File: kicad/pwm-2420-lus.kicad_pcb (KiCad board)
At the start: 2 copper layers, 90 x 85 mm, 127 parts, among them J1 MKDS 5/ 2-9,5, J2 MKDS 5/ 2-9,5, J3 MKDS 5/ 2-9,5, J4 UEXT, J5 USB_A, J6 PWR_12V, J7 6P6C, J8 ST_Nucleo_SWD_5p, Q1 PSMN7R5-60YLX, Q2 PSMN7R5-60YLX, Q3 PSMN7R5-60YLX, Q6 IRFB7787, Q7 IRFB7787, Q8 IRFB7787, T1 MMBT3904, T2 MMBT3906, T3 MMBT3904, T4 MMBT3904, T5 MMBT3904, U1 STM32L072CZTx, U2 TLV9002, U3 MC34063AD, U4 D1213A-04SO, U5 LP2950-3.3_TO252

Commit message: Folder restructured and files renamed
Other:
- board text removed: "~RESET"

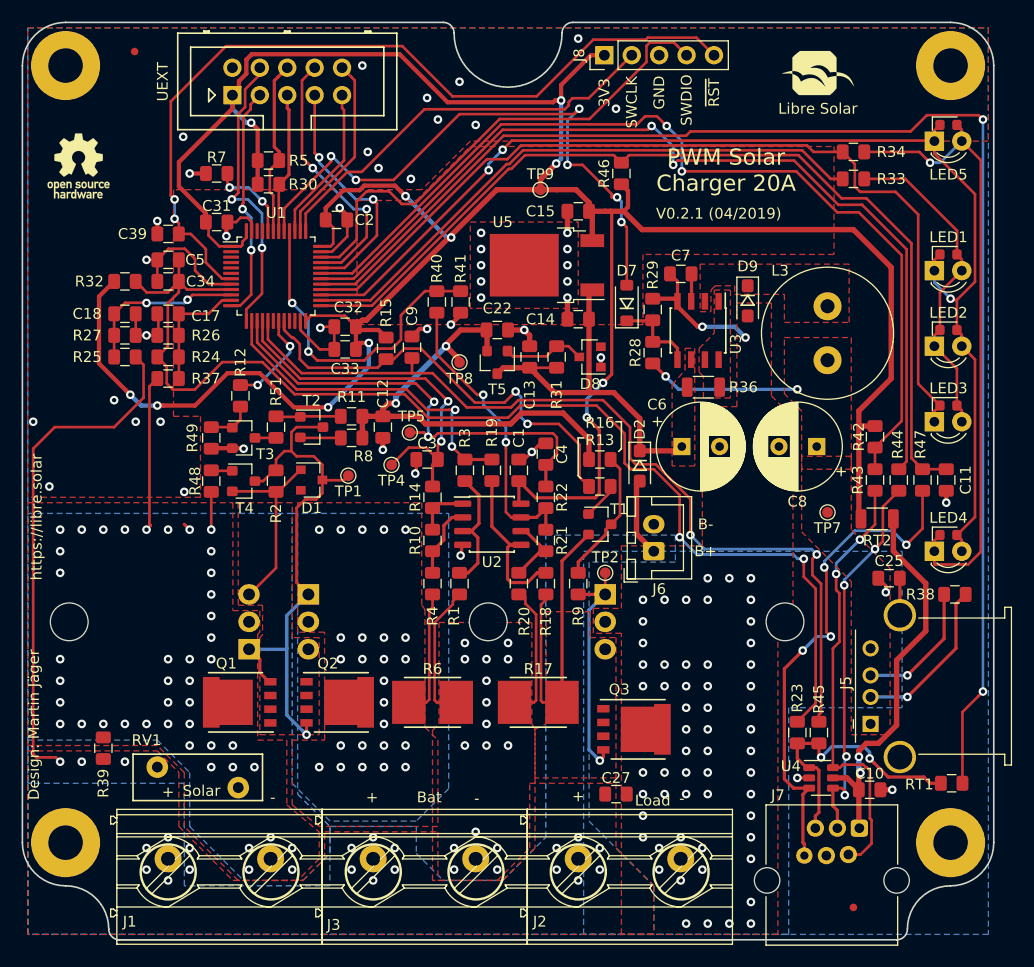
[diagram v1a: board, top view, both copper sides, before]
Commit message: Load current sense filter and comparator updated
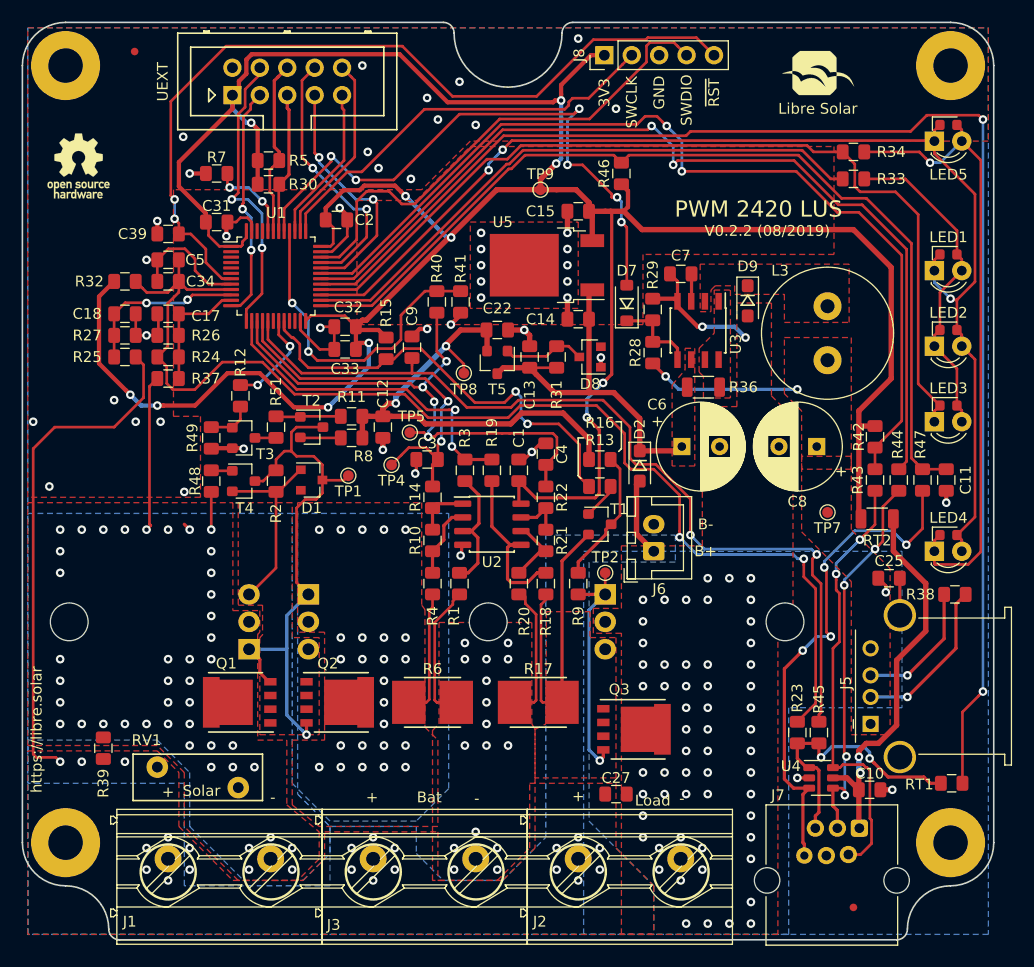
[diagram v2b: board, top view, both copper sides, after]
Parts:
- R22: value 2.2k -> 39k
- moved TP8 1.08 mm to (139.4, 85.5)
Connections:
- R40 pad 2: Net-(R21-Pad2) -> I_LOAD
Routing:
- net Net-(R21-Pad2): track 27.8 -> 4.76 mm, vias 2 -> 0
- net I_LOAD: track 43.2 -> 51.6 mm, vias 2 -> 4
- net +12V: track 44.4 -> 45.5 mm
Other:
- board text added: "PWM 2420 LUS"
- board text added: "V0.2.2 (08/2019)"
- board text removed: "Design: Martin Jäger"
- board text removed: "PWM Solar Charger 20A"
- board text removed: "V0.2.1 (04/2019)"
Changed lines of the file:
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@@
-(kicad_pcb (version 20171130) (host pcbnew 5.1.0)
+(kicad_pcb (version 20171130) (host pcbnew 5.1.2)
   (general
     (thickness 1.6)
-    (drawings 81)
-    (tracks 1282)
+    (drawings 80)
+    (tracks 1278)
     (zones 0)
     (modules 127)
@@
     )
     (pad 2 smd roundrect (at 1 0 270) (size 1.1 1.4) (layers Top F.Paste F.Mask) (roundrect_rratio 0.2)
-      (net 52 "Net-(R21-Pad2)"))
+      (net 28 I_LOAD))
     (pad 1 smd roundrect (at -1 0 270) (size 1.1 1.4) (layers Top F.Paste F.Mask) (roundrect_rratio 0.2)
       (net 60 I_LOAD_COMP))
@@
       (effects (font (size 1 1) (thickness 0.15)))
     )
-    (fp_text value 2.2k (at 0 1.75 90) (layer F.Fab)
+    (fp_text value 39k (at 0 1.75 90) (layer F.Fab)
       (effects (font (size 1 1) (thickness 0.15)))
     )
@@
   )
   (module TestPoint:TestPoint_Pad_D1.0mm (layer Top)
-    (at 139 84.5)
+    (at 139.4 85.5)
     (descr "SMD pad as test Point, diameter 1.0mm")
     (tags "test point SMD pad")
@@
     (effects (font (size 1.5 1.5) (thickness 0.3)) (justify mirror))
   )
-  (gr_text "V0.2.1 (04/2019)" (at 157.2 71.3) (layer F.SilkS)
+  (gr_text "V0.2.2 (08/2019)" (at 161.7 72.9) (layer F.SilkS)
     (effects (font (size 1 1) (thickness 0.15)) (justify left bottom))
   )
-  (gr_text "PWM Solar\nCharger 20A" (at 163.7 66.7) (layer F.SilkS)
+  (gr_text "PWM 2420 LUS" (at 166.7 70.3) (layer F.SilkS)
     (effects (font (size 1.5 1.5) (thickness 0.3)))
   )
@@
   (gr_line (start 107.5 138) (end 179.5 138) (angle 90) (layer Edge.Cuts) (width 0.15))
   (gr_arc (start 102.5 129) (end 102.5 133) (angle 90) (layer Edge.Cuts) (width 0.15))
-  (gr_text "Design: Martin Jäger" (at 100.15 125.05 90) (layer F.SilkS)
-    (effects (font (size 1 1) (thickness 0.15)) (justify left bottom))
-  )
-  (gr_text https://libre.solar (at 100.4 104.7 90) (layer F.SilkS)
+  (gr_text https://libre.solar (at 100.4 124.4 90) (layer F.SilkS)
     (effects (font (size 1 1) (thickness 0.15)) (justify left bottom))
   )
@@
   (segment (start 147 96) (end 147 94) (width 0.3) (layer Top) (net 28))
   (via (at 136.649995 88.149995) (size 0.8) (drill 0.4) (layers Top Bottom) (net 28))
-  (segment (start 134.949991 86.449991) (end 136.299996 87.799996) (width 0.25) (layer Top) (net 28))
-  (segment (start 120.25 82.658002) (end 124.041989 86.449991) (width 0.25) (layer Top) (net 28))
-  (segment (start 124.041989 86.449991) (end 134.949991 86.449991) (width 0.25) (layer Top) (net 28))
-  (segment (start 136.299996 87.799996) (end 136.649995 88.149995) (width 0.25) (layer Top) (net 28))
-  (segment (start 120.25 80.6625) (end 120.25 82.658002) (width 0.25) (layer Top) (net 28))
-  (segment (start 136.1 90.90503) (end 136.1 91.400004) (width 0.25) (layer Bottom) (net 28))
-  (segment (start 136.1 88.69999) (end 136.1 90.90503) (width 0.25) (layer Bottom) (net 28))
   (segment (start 135.750001 91.050005) (end 136.1 91.400004) (width 0.25) (layer Top) (net 28))
   (segment (start 135.699996 91) (end 135.750001 91.050005) (width 0.25) (layer Top) (net 28))
   (segment (start 134.4 91) (end 135.699996 91) (width 0.25) (layer Top) (net 28))
   (via (at 136.1 91.400004) (size 0.8) (drill 0.4) (layers Top Bottom) (net 28))
-  (segment (start 136.649995 88.149995) (end 136.1 88.69999) (width 0.25) (layer Bottom) (net 28))
   (segment (start 136.990666 91.075023) (end 136.665685 91.400004) (width 0.25) (layer Top) (net 28))
   (segment (start 136.665685 91.400004) (end 136.1 91.400004) (width 0.25) (layer Top) (net 28))
@@
   (segment (start 147 94) (end 148.02501 92.97499) (width 0.25) (layer Top) (net 28))
   (segment (start 143.648002 91.074998) (end 142.951998 91.074998) (width 0.25) (layer Top) (net 28))
+  (via (at 137.8 84.4) (size 0.8) (drill 0.4) (layers Top Bottom) (net 28))
+  (segment (start 137.8 84.4) (end 135.6 86.6) (width 0.25) (layer Bottom) (net 28))
+  (via (at 135.6 86.8) (size 0.8) (drill 0.4) (layers Top Bottom) (net 28))
+  (segment (start 135.6 86.6) (end 135.6 86.8) (width 0.25) (layer Bottom) (net 28))
+  (segment (start 136.649995 87.849995) (end 135.6 86.8) (width 0.25) (layer Top) (net 28))
+  (segment (start 136.649995 88.149995) (end 136.649995 87.849995) (width 0.25) (layer Top) (net 28))
+  (segment (start 134.8 86.8) (end 135.6 86.8) (width 0.25) (layer Top) (net 28))
+  (segment (start 134.449991 86.449991) (end 134.8 86.8) (width 0.25) (layer Top) (net 28))
+  (segment (start 124.041989 86.449991) (end 134.449991 86.449991) (width 0.25) (layer Top) (net 28))
+  (segment (start 120.25 80.6625) (end 120.25 82.658002) (width 0.25) (layer Top) (net 28))
+  (segment (start 120.25 82.658002) (end 124.041989 86.449991) (width 0.25) (layer Top) (net 28))
+  (segment (start 136.1 90.90503) (end 136.1 91.400004) (width 0.25) (layer Bottom) (net 28))
+  (segment (start 136.7 90.30503) (end 136.1 90.90503) (width 0.25) (layer Bottom) (net 28))
+  (segment (start 136.649995 88.149995) (end 136.7 88.2) (width 0.25) (layer Bottom) (net 28))
+  (segment (start 136.7 88.2) (end 136.7 90.30503) (width 0.25) (layer Bottom) (net 28))
+  (segment (start 136.9 83.5) (end 137.8 84.4) (width 0.25) (layer Top) (net 28))
+  (segment (start 136.9 79.9) (end 136.9 83.5) (width 0.25) (layer Top) (net 28))
   (segment (start 143.940501 83.940501) (end 143.45 83.45) (width 0.25) (layer Top) (net 29))
   (segment (start 147.059499 83.940501) (end 143.940501 83.940501) (width 0.25) (layer Top) (net 29))
@@
   (segment (start 146.135 98.865) (end 147 98) (width 0.3) (layer Top) (net 52))
   (segment (start 144.6 98.865) (end 146.135 98.865) (width 0.3) (layer Top) (net 52))
-  (via (at 141.2 87.499996) (size 0.8) (drill 0.4) (layers Top Bottom) (net 52))
-  (segment (start 136.9 79.9) (end 136.9 83.765681) (width 0.25) (layer Top) (net 52))
-  (segment (start 136.9 83.765681) (end 140.634315 87.499996) (width 0.25) (layer Top) (net 52))
-  (segment (start 140.634315 87.499996) (end 141.2 87.499996) (width 0.25) (layer Top) (net 52))
-  (segment (start 144.7 98.865) (end 143.8 98.865) (width 0.25) (layer Top) (net 52))
-  (segment (start 143.8 98.865) (end 143.3 98.365) (width 0.25) (layer Top) (net 52))
-  (segment (start 143.3 92.465689) (end 143.3 91.900004) (width 0.25) (layer Top) (net 52))
-  (segment (start 143.3 98.365) (end 143.3 92.465689) (width 0.25) (layer Top) (net 52))
-  (via (at 143.3 91.900004) (size 0.8) (drill 0.4) (layers Top Bottom) (net 52))
-  (segment (start 143.3 91.334319) (end 143.3 91.900004) (width 0.25) (layer Bottom) (net 52))
-  (segment (start 143.3 90.5) (end 143.3 91.334319) (width 0.25) (layer Bottom) (net 52))
-  (segment (start 141.2 87.499996) (end 141.2 88.4) (width 0.25) (layer Bottom) (net 52))
-  (segment (start 141.2 88.4) (end 143.3 90.5) (width 0.25) (layer Bottom) (net 52))
   (via (at 132 114) (size 0.8) (drill 0.4) (layers Top Bottom) (net 53))
   (via (at 132 116) (size 0.8) (drill 0.4) (layers Top Bottom) (net 53))
@@
   (segment (start 141.55 81.55) (end 141.5 81.5) (width 0.5) (layer Top) (net 79))
   (segment (start 141.55 83.45) (end 141.55 81.55) (width 0.5) (layer Top) (net 79))
-  (segment (start 139 84.25) (end 137.75 83) (width 0.5) (layer Top) (net 79))
-  (segment (start 139 84.5) (end 139 84.25) (width 0.5) (layer Top) (net 79))
   (segment (start 141.5 81.5) (end 139.1 81.5) (width 0.5) (layer Top) (net 79))
   (segment (start 137.75 82.85) (end 137.75 83) (width 0.5) (layer Top) (net 79))
@@
   (segment (start 151 91.6) (end 148.599998 89.199998) (width 0.5) (layer Top) (net 79))
   (segment (start 135.150401 89.5) (end 132.7 89.5) (width 0.5) (layer Top) (net 79))
+  (segment (start 139.4 84.65) (end 137.75 83) (width 0.25) (layer Top) (net 79))
+  (segment (start 139.4 85.5) (end 139.4 84.65) (width 0.25) (layer Top) (net 79))
   (segment (start 185.54 62.9525) (end 185.0875 62.5) (width 0.25) (layer Top) (net 80))
   (segment (start 185.54 64) (end 185.54 62.9525) (width 0.25) (layer Top) (net 80))

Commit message: Improved power supply and exposed BOOT0 pin
- BOOT0 pin connected to BUTTON wire to allow firmware upgrade via LS.one port
- Additional emitter follower for 3V3 power supply to increase margin to 30V absolute max. rating of LDO in case of 24V battery
- Corners adjusted to match shape of MPPT 1210 HUS
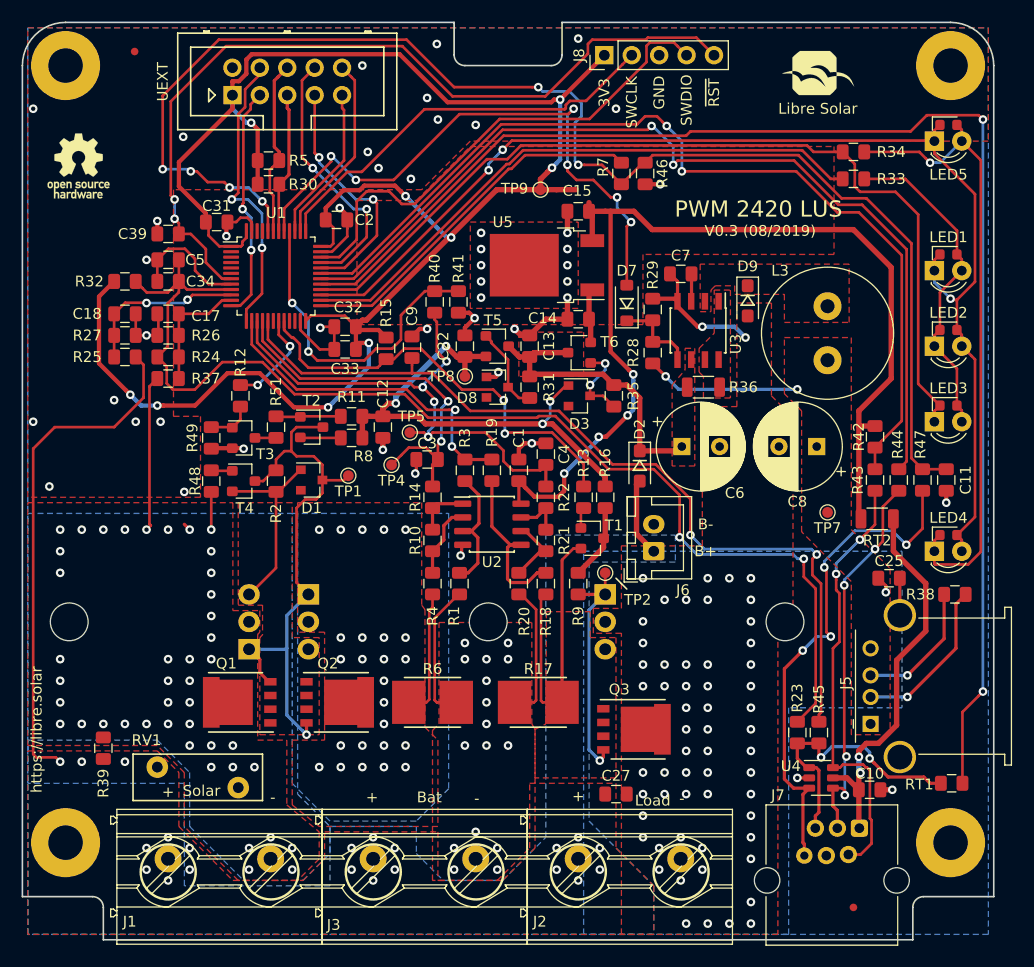
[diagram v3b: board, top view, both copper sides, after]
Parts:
- added D3: 12V, Diode_SMD:D_SOT-23_ANK, F.Cu at (150.1, 87.6)
- added R35: 12k, LibreSolar:R_0805_2012, F.Cu at (153.3, 87.6)
- added T6: MMBT3904, LibreSolar:SOT-23, F.Cu at (150.1, 83.6)
- Q6, Q7, Q8: value IRFB7787 -> AOT266L
- moved R7 37.5 mm to (154.0, 67.0), turned to 270 degrees
- moved D8 9.04 mm to (142.5, 86.8), turned to 0 degrees
- moved R31 3.75 mm to (145.5, 86.8), turned to 90 degrees
- moved R16 3.54 mm to (152.5, 97.0), turned to 90 degrees
- moved C22 3.35 mm to (139.5, 83.0), turned to 90 degrees
- moved R46 2.20 mm to (156.2, 67.0), turned to 270 degrees
- moved R13 1.80 mm to (150.5, 97.0), turned to 90 degrees
- moved T5 1.50 mm to (142.5, 83.0), turned to 0 degrees
- moved T1 1.48 mm to (151.3, 100.8)
- moved C13 1.00 mm to (145.5, 83.0)
- moved TP8 0.32 mm to (139.5, 85.8)
- moved R40 0.20 mm to (136.7, 78.9)
- moved R41 0.20 mm to (138.9, 78.9)
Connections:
- C11 pad 1: /MCU/BUTTON -> /MCU/BOOT0
- C13 pad 1: Net-(C13-Pad1) -> /Power Supply/BAT_INPUT
- C14 pad 1: Net-(C13-Pad1) -> Net-(C14-Pad1)
- C6 pad 1: Net-(C13-Pad1) -> /Power Supply/BAT_INPUT
- D2 pad 1: Net-(C13-Pad1) -> /Power Supply/BAT_INPUT
- MK2 pad 1: GND -> Net-(MK2-Pad1)
- MK3 pad 1: GND -> Net-(MK3-Pad1)
- MK4 pad 1: GND -> Net-(MK4-Pad1)
- R31 pad 2: Net-(C13-Pad1) -> /Power Supply/BAT_INPUT
- R36 pad 2: Net-(C13-Pad1) -> /Power Supply/BAT_INPUT
- R46 pad 1: +3V3 -> /MCU/BOOT0
- R46 pad 2: /MCU/BUTTON -> GND
- R47 pad 2: /MCU/BUTTON -> /MCU/BOOT0
- R7 pad 1: /MCU/BOOT0 -> /MCU/BUTTON
- R7 pad 2: GND -> /MCU/BOOT0
- T5 pad 3: Net-(C13-Pad1) -> /Power Supply/BAT_INPUT
- U3 pad 6: Net-(C13-Pad1) -> /Power Supply/BAT_INPUT
- U5 pad 1: Net-(C13-Pad1) -> Net-(C14-Pad1)
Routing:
- net /MCU/BOOT0: track 7.92 -> 129.4 mm, vias 2 -> 6
- net /MCU/BUTTON: track 88.0 -> 33.9 mm
- net Net-(C13-Pad1): track 34.6 -> 0.00 mm
- net /Power Supply/BAT_INPUT: track 0.00 -> 28.0 mm
- net Net-(D3-Pad1): track 0.00 -> 7.56 mm, vias 0 -> 2
- net GND: track 89.6 -> 96.0 mm, vias 62 -> 63
- net +3V3: track 283.1 -> 277.1 mm, vias 11 -> 13
- net Net-(R16-Pad1): track 12.5 -> 7.04 mm
- net Net-(C14-Pad1): track 0.00 -> 5.06 mm
- net VDDA: track 111.6 -> 109.2 mm
- net +12V: track 45.5 -> 47.8 mm, vias 2 -> 4
- net T_BAT: track 82.5 -> 80.3 mm
- net I_LOAD: track 51.6 -> 49.8 mm
- net Net-(R13-Pad1): track 3.40 -> 1.95 mm
- net LOAD_DIS: track 41.1 -> 39.9 mm
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- added copper zone on F.Cu, net /Power Supply/BAT_INPUT
- removed copper zone on F.Cu, net Net-(C13-Pad1)
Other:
- outline, holes or cut-outs redrawn
- board text added: "V0.3 (08/2019)"
- board text removed: "V0.2.2 (08/2019)"
